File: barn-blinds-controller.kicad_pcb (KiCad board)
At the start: 4 copper layers, 65 x 60 mm, 72 parts, among them J1 DC005-T25, J2 Screw_Terminal_01x02, J3 Screw_Terminal_01x02, J4 Screw_Terminal_01x02, J5 Screw_Terminal_01x02, J6 KH-TYPE-C-16P (Kinghelm), SW1 BOOT, SW2 RESET, U1 ESP32-S3-WROOM-1, U10 ACS723xLCTR-05AB, U11 TMP235, U2 TB6612FNG, U3 TB6612FNG, U4 ISO7760DBQ, U5 ISO7760DBQ, U6 ISO7760DBQ, U7 DCDC Converter, U8 AP2112K-3.3, U9 AMS1117-3.3

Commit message: Started running traces
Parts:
- moved R5 27.6 mm to (85.5, 101.0)
- moved R6 27.6 mm to (85.5, 103.0)
- moved C20 26.3 mm to (118.2, 103.0), turned to 180 degrees
- moved C_ISO_F1 19.4 mm to (119.6, 82.0)
- moved C40 18.6 mm to (115.7, 78.6)
- moved R4 16.8 mm to (83.0, 73.7)
- moved R3 16.8 mm to (83.0, 72.5)
- moved C_ISO_A1 16.3 mm to (102.9, 67.7), turned to 0 degrees
- moved SW1 15.1 mm to (102.8, 74.0)
- moved C_ACS2 14.9 mm to (92.6, 73.6), turned to 90 degrees
- moved R_BOOT1 13.4 mm to (99.8, 77.0), turned to 0 degrees
- moved C_VCC_A1 9.77 mm to (110.5, 59.8)
- moved C_VCC_A2 9.77 mm to (110.5, 61.8)
- moved R9 9.76 mm to (119.6, 83.5)
- moved C_VM_A1 9.53 mm to (115.8, 71.5)
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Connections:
- C40 pad 2: GND_POWER -> GND_MOTOR
- C41 pad 2: GND_POWER -> GND_MOTOR
- C_VCC_A1 pad 2: GND_POWER -> GND_MOTOR
- C_VCC_A2 pad 2: GND_POWER -> GND_MOTOR
- C_VCC_B1 pad 2: GND_POWER -> GND_MOTOR
- C_VCC_B2 pad 2: GND_POWER -> GND_MOTOR
- U1 pad 12: /ISO_M4_CLOSE -> unconnected-(U1-GPIO8/TOUCH8/ADC1_CH7/SUBSPICS1-Pad12)
- U1 pad 15: /ISO_M2_OPEN -> unconnected-(U1-GPIO3/TOUCH3/ADC1_CH2-Pad15)
- U1 pad 17: /ISO_STBY -> unconnected-(U1-GPIO9/TOUCH9/ADC1_CH8/FSPIHD/SUBSPIHD-Pad17)
- U1 pad 18: /ISO_PWM_M1 -> unconnected-(U1-GPIO10/TOUCH10/ADC1_CH9/FSPICS0/FSPIIO4/SUBSPICS0-Pad18)
- U1 pad 19: /ISO_PWM_M2 -> unconnected-(U1-GPIO11/TOUCH11/ADC2_CH0/FSPID/FSPIIO5/SUBSPID-Pad19)
- U1 pad 20: /ISO_PWM_M3 -> unconnected-(U1-GPIO12/TOUCH12/ADC2_CH1/FSPICLK/FSPIIO6/SUBSPICLK-Pad20)
- U1 pad 21: /ISO_PWM_M4 -> unconnected-(U1-GPIO13/TOUCH13/ADC2_CH2/FSPIQ/FSPIIO7/SUBSPIQ-Pad21)
- U1 pad 26: unconnected-(U1-GPIO45-Pad26) -> /ISO_PWM_M4
- U1 pad 28: unconnected-(U1-SPIIO6/GPIO35/FSPID/SUBSPID-Pad28) -> /ISO_PWM_M3
- U1 pad 29: unconnected-(U1-SPIIO7/GPIO36/FSPICLK/SUBSPICLK-Pad29) -> /ISO_PWM_M2
- U1 pad 30: unconnected-(U1-SPIDQS/GPIO37/FSPIQ/SUBSPIQ-Pad30) -> /ISO_PWM_M1
- U1 pad 31: unconnected-(U1-GPIO38/FSPIWP/SUBSPIWP-Pad31) -> /ISO_STBY
- U1 pad 32: unconnected-(U1-MTCK/GPIO39/CLK_OUT3/SUBSPICS1-Pad32) -> /ISO_M4_CLOSE
- U1 pad 33: unconnected-(U1-MTDO/GPIO40/CLK_OUT2-Pad33) -> /ISO_M4_OPEN
- U1 pad 34: unconnected-(U1-MTDI/GPIO41/CLK_OUT1-Pad34) -> /ISO_M3_CLOSE
- U1 pad 35: unconnected-(U1-MTMS/GPIO42-Pad35) -> /ISO_M3_OPEN
- U1 pad 36: unconnected-(U1-U0RXD/GPIO44/CLK_OUT2-Pad36) -> /ISO_M2_CLOSE
- U1 pad 37: unconnected-(U1-U0TXD/GPIO43/CLK_OUT1-Pad37) -> /ISO_M2_OPEN
- U1 pad 4: /ISO_M2_CLOSE -> unconnected-(U1-GPIO4/TOUCH4/ADC1_CH3-Pad4)
- U1 pad 5: /ISO_M3_OPEN -> unconnected-(U1-GPIO5/TOUCH5/ADC1_CH4-Pad5)
- U1 pad 6: /ISO_M3_CLOSE -> unconnected-(U1-GPIO6/TOUCH6/ADC1_CH5-Pad6)
- U1 pad 7: /ISO_M4_OPEN -> unconnected-(U1-GPIO7/TOUCH7/ADC1_CH6-Pad7)
- U2 pad 18: GND_POWER -> GND_MOTOR
- U3 pad 18: GND_POWER -> GND_MOTOR
- U9 pad 1: GND_POWER -> GND_MOTOR
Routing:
- net +3.3V_MOTOR: track 0.00 -> 38.8 mm, vias 0 -> 9
- net Net-(J6-D--PadA7): track 0.00 -> 36.7 mm, vias 0 -> 1
- net Net-(J6-D+-PadA6): track 0.00 -> 35.3 mm, vias 0 -> 1
- net /STBY: track 0.00 -> 32.3 mm, vias 0 -> 3
- net /PWM_M2: track 0.00 -> 20.4 mm, vias 0 -> 1
- net /ISO_PWM_M4: track 0.00 -> 18.9 mm
- net Net-(U1-EN): track 0.00 -> 16.3 mm, vias 0 -> 1
- net /ISO_M3_CLOSE: track 0.00 -> 13.6 mm
- net /ISO_M3_OPEN: track 0.00 -> 13.1 mm
- net /ISO_STBY: track 0.00 -> 13.0 mm
- net /ISO_M4_CLOSE: track 0.00 -> 12.3 mm
- net /ISO_M2_CLOSE: track 0.00 -> 12.3 mm
- net +12V_RAW: track 24.4 -> 36.4 mm, vias 0 -> 1
- net /ISO_M4_OPEN: track 0.00 -> 11.9 mm
- net /ISO_M2_OPEN: track 0.00 -> 11.6 mm
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
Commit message: PCB tracing complete
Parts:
- moved U11 20.2 mm to (104.1, 57.6), turned to -90 degrees
- moved R9 12.5 mm to (119.2, 71.0)
- moved U9 11.6 mm to (110.4, 54.0), turned to 90 degrees
- moved R10 9.41 mm to (122.2, 72.6)
- moved C1 9.10 mm to (122.0, 56.0)
- moved U2 9.08 mm to (122.0, 65.5)
- moved U6 8.64 mm to (110.4, 75.6)
- moved U4 8.63 mm to (110.4, 62.6)
- moved U5 8.63 mm to (110.4, 69.0)
- moved C2 8.52 mm to (122.0, 84.5)
- moved U3 8.44 mm to (122.0, 75.1)
- moved R8 7.93 mm to (124.6, 61.8), turned to 90 degrees
- moved R7 7.14 mm to (121.2, 63.0), turned to 180 degrees
- moved R1 3.32 mm to (121.3, 60.8), turned to 180 degrees
- moved C_VCC_B2 2.80 mm to (119.2, 74.0)
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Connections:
- D4 pad 1: /Motor Outputs/U2_A02 -> U2_A02
- D5 pad 1: /Motor Outputs/U2_B02 -> U2_B02
- D6 pad 1: /Motor Outputs/U3_A02 -> U3_A02
- D7 pad 1: /Motor Outputs/U3_B02 -> U3_B02
- F1 pad 1: /Motor Outputs/U2_A01 -> U2_A01
- F2 pad 1: /Motor Outputs/U2_B01 -> U2_B01
- F3 pad 2: /Motor Outputs/U3_A01 -> U3_A01
- F4 pad 1: /Motor Outputs/U3_B01 -> U3_B01
- J2 pad 2: /Motor Outputs/U2_A02 -> U2_A02
- J3 pad 2: /Motor Outputs/U2_B02 -> U2_B02
- J4 pad 2: /Motor Outputs/U3_A02 -> U3_A02
- J5 pad 2: /Motor Outputs/U3_B02 -> U3_B02
- U1 pad 26: /ISO_PWM_M4 -> /ISO_STBY
- U1 pad 28: /ISO_PWM_M3 -> /ISO_PWM_M4
- U1 pad 29: /ISO_PWM_M2 -> /ISO_M4_CLOSE
- U1 pad 30: /ISO_PWM_M1 -> /ISO_M4_OPEN
- U1 pad 31: /ISO_STBY -> /ISO_M3_OPEN
- U1 pad 32: /ISO_M4_CLOSE -> /ISO_M3_CLOSE
- U1 pad 33: /ISO_M4_OPEN -> /ISO_PWM_M3
- U1 pad 34: /ISO_M3_CLOSE -> /ISO_PWM_M2
- U1 pad 35: /ISO_M3_OPEN -> /ISO_M2_CLOSE
- U1 pad 36: /ISO_M2_CLOSE -> /ISO_M2_OPEN
- U1 pad 37: /ISO_M2_OPEN -> /ISO_PWM_M1
- U2 pad 1: /U2_A01 -> U2_A01
- U2 pad 11: /U2_B01 -> U2_B01
- U2 pad 12: /U2_B01 -> U2_B01
- U2 pad 16: /M3_BIN2 -> /M2_BIN2
- U2 pad 2: /U2_A01 -> U2_A01
- U2 pad 5: /U2_A02 -> U2_A02
- U2 pad 6: /U2_A02 -> U2_A02
- U2 pad 7: /U2_B02 -> U2_B02
- U2 pad 8: /U2_B02 -> U2_B02
- U3 pad 1: /U3_A01 -> U3_A01
- U3 pad 11: /U3_B01 -> U3_B01
- U3 pad 12: /U3_B01 -> U3_B01
- U3 pad 2: /U3_A01 -> U3_A01
- U3 pad 5: /U3_A02 -> U3_A02
- U3 pad 6: /U3_A02 -> U3_A02
- U3 pad 7: /U3_B02 -> U3_B02
- U3 pad 8: /U3_B02 -> U3_B02
- U4 pad 10: /M3_AIN2 -> /PWM_M2
- U4 pad 11: /M3_AIN1 -> /M2_BIN2
- U4 pad 12: /M2_BIN2 -> /M2_BIN1
- U4 pad 13: /M2_BIN1 -> /PWM_M1
- U4 pad 4: /ISO_M2_OPEN -> /ISO_PWM_M1
- U4 pad 5: /ISO_M2_CLOSE -> /ISO_M2_OPEN
- U4 pad 6: /ISO_M3_OPEN -> /ISO_M2_CLOSE
- U4 pad 7: /ISO_M3_CLOSE -> /ISO_PWM_M2
- U5 pad 10: unconnected-(U5-OUTF-Pad10) -> /PWM_M4
- U5 pad 11: unconnected-(U5-OUTE-Pad11) -> /M4_BIN2
- U5 pad 12: unconnected-(U5-OUTD-Pad12) -> /M4_BIN1
- U5 pad 13: /STBY -> /M3_AIN1
- U5 pad 14: /M4_BIN2 -> /M3_AIN2
- U5 pad 15: /M4_BIN1 -> /PWM_M3
- U5 pad 2: /ISO_M4_OPEN -> /ISO_PWM_M3
- U5 pad 3: /ISO_M4_CLOSE -> /ISO_M3_CLOSE
- U5 pad 4: /ISO_STBY -> /ISO_M3_OPEN
- U5 pad 5: GND_ISO -> /ISO_M4_OPEN
- U5 pad 6: GND_ISO -> /ISO_M4_CLOSE
- U5 pad 7: GND_ISO -> /ISO_PWM_M4
- U6 pad 12: /PWM_M4 -> unconnected-(U6-OUTD-Pad12)
- U6 pad 13: /PWM_M3 -> unconnected-(U6-OUTC-Pad13)
- U6 pad 14: /PWM_M2 -> unconnected-(U6-OUTB-Pad14)
- U6 pad 15: /PWM_M1 -> /STBY
- U6 pad 2: /ISO_PWM_M1 -> /ISO_STBY
- U6 pad 3: /ISO_PWM_M2 -> GND_ISO
- U6 pad 4: /ISO_PWM_M3 -> GND_ISO
- U6 pad 5: /ISO_PWM_M4 -> GND_ISO
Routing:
- net U3_B02: track 0.00 -> 31.7 mm, vias 0 -> 1
- net /GPIO15: track 0.00 -> 26.2 mm
- net U2_A02: track 0.00 -> 26.0 mm, vias 0 -> 1
- net U2_A01: track 0.00 -> 24.8 mm, vias 0 -> 1
- net GND_MOTOR: track 9.68 -> 33.2 mm, vias 26 -> 27
- net +3.3V_MOTOR: track 38.8 -> 15.7 mm, vias 9 -> 15
- net U3_A02: track 0.00 -> 21.2 mm, vias 0 -> 1
- net +12V: track 9.65 -> 30.7 mm, vias 10 -> 16
- net /GPIO14: track 0.64 -> 20.9 mm
- net U2_B02: track 0.00 -> 18.0 mm, vias 0 -> 1
- net /PWM_M4: track 2.17 -> 19.7 mm
- net /M4_BIN2: track 0.00 -> 16.7 mm
- net /M4_BIN1: track 0.00 -> 15.7 mm
- net /M2_BIN2: track 0.00 -> 13.7 mm
- net /M3_AIN1: track 0.00 -> 13.3 mm
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
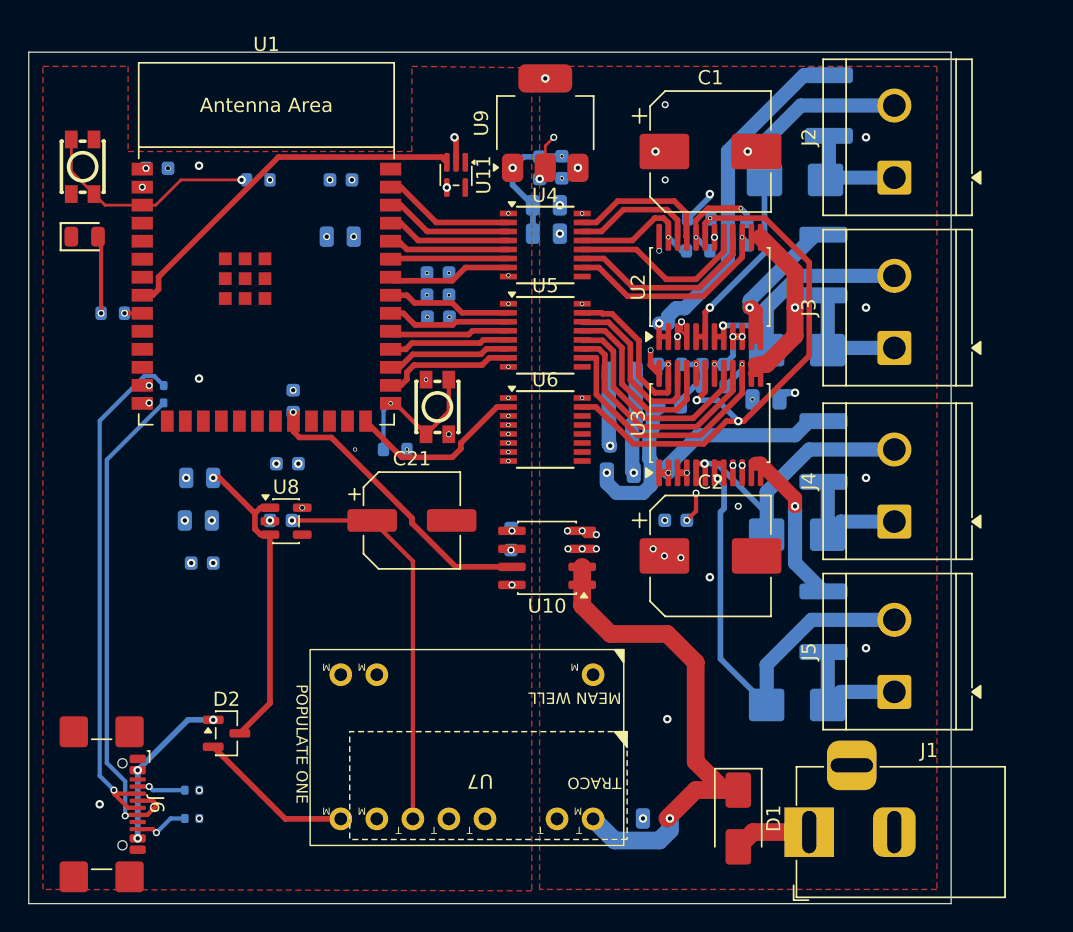
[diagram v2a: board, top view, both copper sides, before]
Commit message: Reworking with new terminal block, adding mounting holes.  Need to rerun a number of traces.
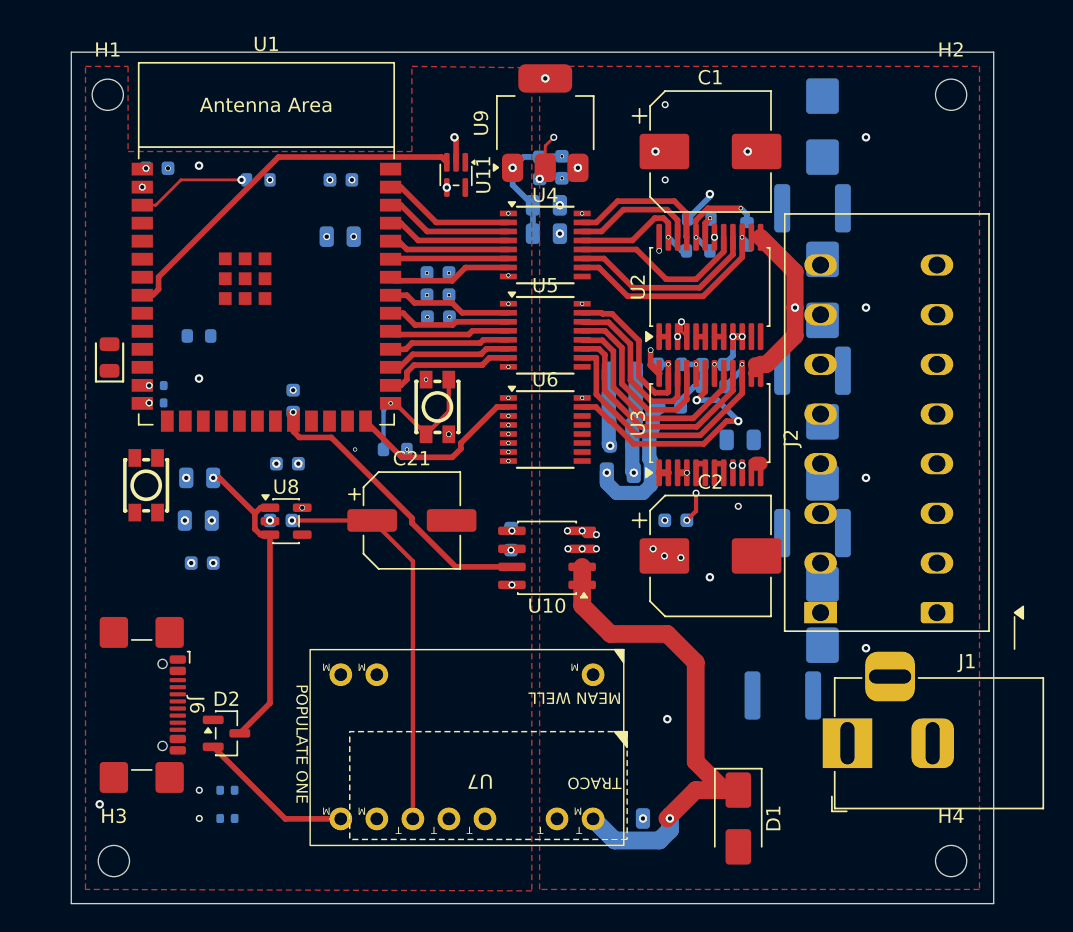
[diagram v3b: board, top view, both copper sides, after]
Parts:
- removed J3, J4, J5: Screw_Terminal_01x02, TerminalBlock_CUI:TerminalBlock_CUI_TB007-508-02_1x02_P5.08mm_Horizontal
- added H1: MountingHole, MountingHole:MountingHole_2.2mm_M2, F.Cu at (79.6, 52.0)
- added H2: MountingHole, MountingHole:MountingHole_2.2mm_M2, F.Cu at (139.0, 52.0)
- added H3: MountingHole, MountingHole:MountingHole_2.2mm_M2, F.Cu at (80.0, 106.0)
- added H4: MountingHole, MountingHole:MountingHole_2.2mm_M2, F.Cu at (139.0, 106.0)
- J2: value Screw_Terminal_01x02 -> Conn_01x08; footprint TerminalBlock_CUI:TerminalBlock_CUI_TB007-508-02_1x02_P5.08mm_Horizontal -> barn_shade_controller:TerminalBlock_JL271R-35008G01_Spring_1x08_P3.50mm_Horizontal
- moved J2 30.8 mm to (138.0, 88.5)
- moved SW2 22.9 mm to (82.3, 79.5)
- moved D3 8.69 mm to (79.7, 70.5), turned to 90 degrees
- moved J6 7.55 mm to (80.8, 95.0)
- moved F2 7.48 mm to (129.2, 71.4), turned to 0 degrees
- moved F1 7.33 mm to (129.2, 60.0), turned to 0 degrees
- moved J1 6.81 mm to (131.7, 97.7)
- moved D7 6.61 mm to (129.9, 88.6), turned to -90 degrees
- moved R_LED1 6.28 mm to (86.0, 69.0)
- moved D6 6.07 mm to (129.9, 77.2), turned to -90 degrees
- moved F4 5.93 mm to (127.1, 94.3), turned to 0 degrees
- moved F3 5.80 mm to (129.2, 82.9), turned to 180 degrees
- moved D5 4.61 mm to (129.9, 65.8), turned to -90 degrees
- moved D4 4.22 mm to (129.9, 54.2), turned to -90 degrees
- moved C41 3.38 mm to (124.1, 76.3)
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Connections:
- D4 pad 1: U2_A02 -> U2_A01
- D4 pad 2: Net-(J2-Pin_1) -> Net-(J2-Pin_7)
- D5 pad 2: Net-(J3-Pin_1) -> Net-(J2-Pin_6)
- D6 pad 2: Net-(J4-Pin_1) -> Net-(J2-Pin_4)
- D7 pad 2: Net-(J5-Pin_1) -> Net-(J2-Pin_2)
- F1 pad 1: U2_A01 -> U2_A02
- F1 pad 2: Net-(J2-Pin_1) -> Net-(J2-Pin_7)
- F2 pad 2: Net-(J3-Pin_1) -> Net-(J2-Pin_6)
- F3 pad 1: Net-(J4-Pin_1) -> Net-(J2-Pin_4)
- F4 pad 2: Net-(J5-Pin_1) -> Net-(J2-Pin_2)
- J2 pad 1: Net-(J2-Pin_1) -> U3_B02
- J2 pad 2: U2_A02 -> Net-(J2-Pin_2)
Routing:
- net Net-(J6-D--PadA7): track 36.7 -> 0.00 mm, vias 1 -> 0
- net Net-(J6-D+-PadA6): track 35.3 -> 0.00 mm, vias 1 -> 0
- net U3_B02: track 31.7 -> 0.65 mm, vias 1 -> 0
- net U2_A02: track 26.0 -> 0.65 mm, vias 1 -> 0
- net U2_A01: track 24.8 -> 0.65 mm, vias 1 -> 0
- net /STBY: track 41.7 -> 19.9 mm
- net U3_A02: track 21.2 -> 0.65 mm, vias 1 -> 0
- net U2_B02: track 18.0 -> 0.65 mm, vias 1 -> 0
- net U3_A01: track 12.4 -> 0.65 mm, vias 1 -> 0
- net Net-(D2-A): track 11.6 -> 0.00 mm, vias 3 -> 0
- net U3_B01: track 11.2 -> 0.35 mm, vias 1 -> 0
- net U2_B01: track 9.40 -> 0.00 mm, vias 1 -> 0
- net Net-(J5-Pin_1): track 8.93 -> 0.00 mm
- net Net-(J4-Pin_1): track 8.93 -> 0.00 mm
- net Net-(J3-Pin_1): track 8.53 -> 0.00 mm
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
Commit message: Finishing touches
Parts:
- J6: footprint Connector_USB:USB_C_Receptacle_GCT_USB4110 -> barn_shade_controller:KINGHELM_KH-TYPE-C-16P
- R5, R6: moved to F.Cu
- moved F4 10.3 mm to (133.7, 86.4), turned to -90 degrees
- moved R5 7.56 mm to (86.4, 93.6)
- moved R6 6.67 mm to (86.4, 96.5)
- moved R_LED1 6.55 mm to (79.6, 67.7), turned to 90 degrees
- moved C_ISO_F1 5.62 mm to (125.2, 82.0), turned to 0 degrees
- moved F2 5.04 mm to (134.0, 69.8)
- moved F1 5.04 mm to (134.0, 58.4)
- moved F3 4.94 mm to (133.9, 81.2)
- moved D7 4.46 mm to (127.0, 92.0), turned to 0 degrees
- moved D6 4.38 mm to (134.0, 75.6)
- moved D5 4.38 mm to (134.0, 64.1)
- moved D2 4.29 mm to (91.0, 94.0)
- moved D4 3.07 mm to (133.0, 54.0), turned to 0 degrees
- moved R3 2.00 mm to (81.0, 72.5), turned to 0 degrees
- moved R4 1.99 mm to (81.0, 73.8), turned to 0 degrees
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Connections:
- D2 pad 1: Net-(D2-A) -> VBUS
- J6 pad A6: Net-(J6-D+-PadA6) -> /USB-C and 5V Diode-OR/DP
- J6 pad A7: Net-(J6-D--PadA7) -> /USB-C and 5V Diode-OR/DN
- J6 pad B6: Net-(J6-D+-PadA6) -> /USB-C and 5V Diode-OR/DP
- J6 pad B7: Net-(J6-D--PadA7) -> /USB-C and 5V Diode-OR/DN
- R3 pad 1: Net-(J6-D--PadA7) -> /USB-C and 5V Diode-OR/DP
- R4 pad 1: Net-(J6-D+-PadA6) -> /USB-C and 5V Diode-OR/DN
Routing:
- net U2_A01: track 0.65 -> 32.8 mm, vias 0 -> 2
- net /USB-C and 5V Diode-OR/DP: track 0.00 -> 31.7 mm, vias 0 -> 1
- net U2_B02: track 0.65 -> 31.2 mm, vias 0 -> 1
- net /USB-C and 5V Diode-OR/DN: track 0.00 -> 29.8 mm, vias 0 -> 1
- net U3_A02: track 0.65 -> 30.4 mm
- net Net-(J2-Pin_7): track 0.00 -> 28.5 mm
- net U3_B02: track 0.65 -> 28.7 mm, vias 0 -> 1
- net Net-(J2-Pin_6): track 0.00 -> 23.5 mm
- net Net-(U1-EN): track 8.09 -> 30.8 mm
- net /STBY: track 19.9 -> 40.6 mm
- net Net-(J2-Pin_4): track 0.00 -> 20.2 mm
- net Net-(J2-Pin_2): track 0.00 -> 18.1 mm
- net U2_A02: track 0.65 -> 16.3 mm, vias 0 -> 1
- net U3_A01: track 0.65 -> 15.7 mm, vias 0 -> 1
- net VBUS: track 0.00 -> 14.6 mm
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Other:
- board text added: "12V 3A"
- board text added: "ESP32"
- board text added: "ESPHOME 4 SHADE CONTROLLER"
- board text added: "SHADE 1"
- board text added: "SHADE 4"
- board text added: "STATUS LED"
- board text added: "© Tim Irvin 2026"

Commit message: BOM work
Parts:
- removed F1, F2, F3, F4: Polyfuse mSMD110, Fuse:Fuse_1812_4532Metric
- C11: renamed from C1; value 2200uF 25V -> 1000uF 25V; footprint Capacitor_SMD:CP_Elec_8x10 -> Capacitor_SMD:CP_Elec_10x10.5
- C12: renamed from C2; value 2200uF 25V -> 1000uF 25V; footprint Capacitor_SMD:CP_Elec_8x10 -> Capacitor_SMD:CP_Elec_10x10.5
- C4: renamed from C30; value 10uF -> 10uF 10V
- C8: renamed from C33; value 10uF -> 10uF 10V
- C_ACS2: value 10nF -> 10nF 10V
- C_FILT1: value 1nF -> 1nF 10V
- R_LED1: value 470R -> 330R
- moved C11 1.34 mm to (122.1, 54.7)
- moved C12 0.55 mm to (121.4, 85.7), turned to 0 degrees
- renumbered C20 to C1, C41 to C10, C21 to C2, C22 to C3, C31 to C5, C32 to C6, C34 to C7, C40 to C9, D7 to D5, D5 to D6, D6 to D7, H2 to H1, H1 to H2, H4 to H3, H3 to H4, J6 to J2, J2 to J3, R5 to R1, R1 to R10, R4 to R2, R6 to R4, R2 to R5, R7 to R6, R8 to R7, R9 to R8, R10 to R9, SW2 to SW1, SW1 to SW2, U7 to U1, U11 to U10, U10 to U11, U8 to U2, U1 to U3, U9 to U7, U2 to U8, U3 to U9
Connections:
- C10 pad 1: +3.3V_MOTOR -> unconnected-(C10-Pad1)
- C9 pad 1: +12V -> unconnected-(C9-Pad1)
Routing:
- net U2_A02: track 16.3 -> 0.65 mm, vias 1 -> 0
- net U3_A01: track 15.7 -> 0.65 mm, vias 1 -> 0
- net U3_B01: track 11.4 -> 0.65 mm, vias 1 -> 0
- net U2_B01: track 7.56 -> 0.65 mm, vias 1 -> 0
- net Net-(J3-Pin_4): track 20.2 -> 15.8 mm
- net Net-(J3-Pin_7): track 28.5 -> 25.2 mm
- net Net-(J3-Pin_2): track 18.1 -> 19.9 mm
- net +12V: track 29.3 -> 28.4 mm, vias 16 -> 15
- net GND_MOTOR: vias 18 -> 20
- net +3.3V_MOTOR: vias 14 -> 13
